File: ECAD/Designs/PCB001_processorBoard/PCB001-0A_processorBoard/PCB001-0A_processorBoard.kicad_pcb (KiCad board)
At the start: 2 copper layers, 59 parts, among them J1 USB_C_Receptacle_USB2.0_16P, SW1 BSL, SW2 RST, U1 W25Q128JVP, U2 RP2350B-QFN80, U3 BMI323, U4 MMC5983, U5 LG77LC, U6 NRF24L01_Breakout, Y1 ABM8-272-T3

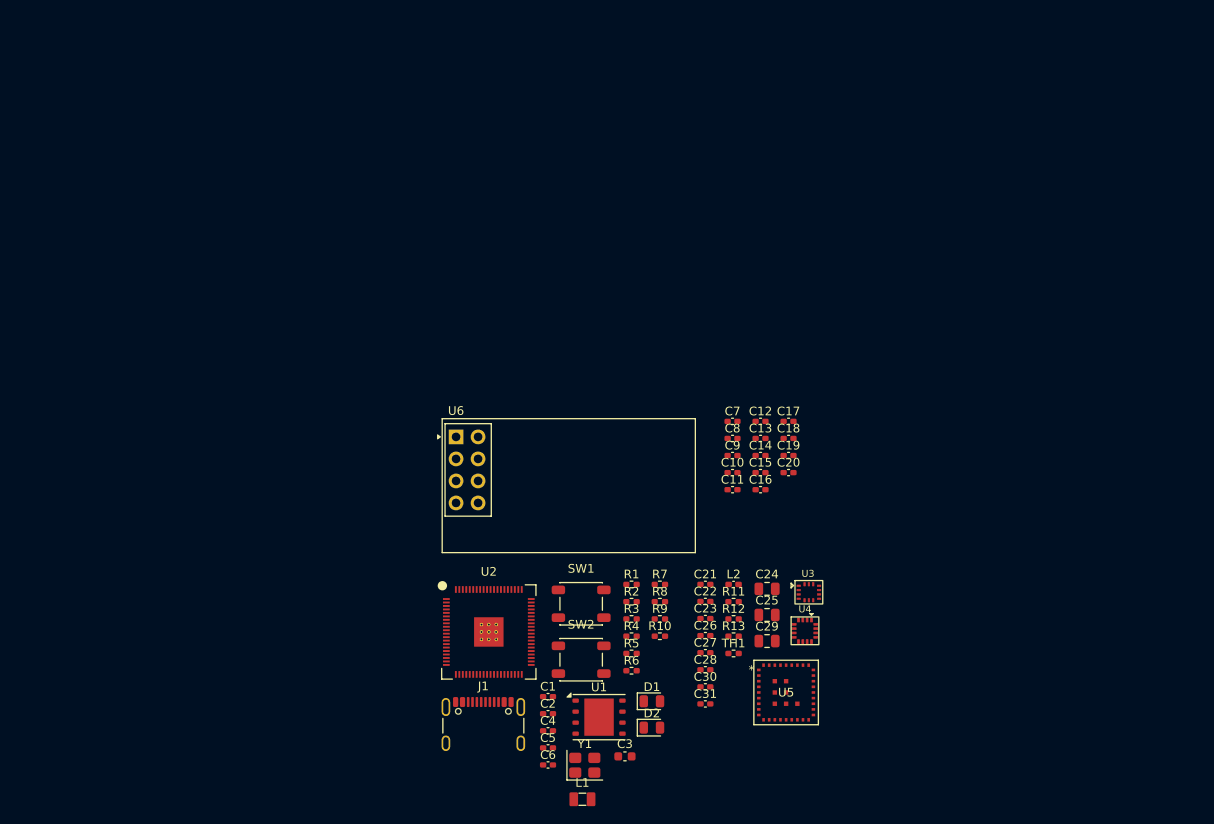
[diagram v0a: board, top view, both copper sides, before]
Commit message: added more connectors to the side of the PCB, added a basic power supply, and began putting parts on the PCB.
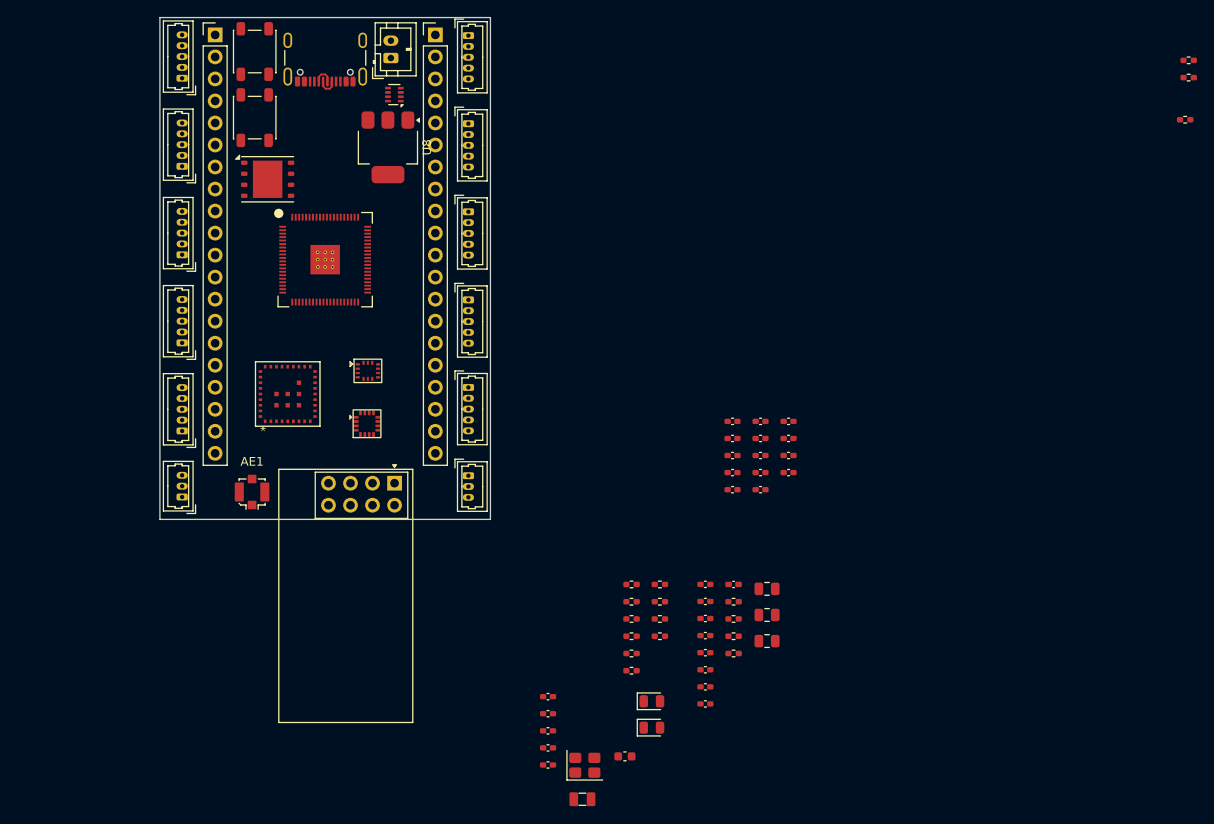
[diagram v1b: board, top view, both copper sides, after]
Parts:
- added AE1: Antenna_Shield, Connector_Coaxial:U.FL_Molex_MCRF_73412-0110_Vertical, F.Cu at (105.9, 101.0)
- added J1: Conn_01x20, Connector_PinHeader_2.54mm:PinHeader_1x20_P2.54mm_Vertical, F.Cu at (101.6, 48.3)
- added J10: ENVIRONMENT, Connector_Molex:Molex_PicoBlade_53047-0510_1x05_P1.25mm_Vertical, F.Cu at (97.8, 93.9)
- added J11: MOTOR0, Connector_Molex:Molex_PicoBlade_53047-0510_1x05_P1.25mm_Vertical, F.Cu at (130.8, 48.3)
- added J12: MOTOR1, Connector_Molex:Molex_PicoBlade_53047-0510_1x05_P1.25mm_Vertical, F.Cu at (130.8, 58.5)
- added J13: MOTOR2, Connector_Molex:Molex_PicoBlade_53047-0510_1x05_P1.25mm_Vertical, F.Cu at (130.8, 68.7)
- added J14: MOTOR3, Connector_Molex:Molex_PicoBlade_53047-0510_1x05_P1.25mm_Vertical, F.Cu at (130.8, 78.8)
- added J15: DISPLAY, Connector_Molex:Molex_PicoBlade_53047-0510_1x05_P1.25mm_Vertical, F.Cu at (130.8, 88.9)
- added J16: EXT_PWR, Connector_JST:JST_PH_B2B-PH-K_1x02_P2.00mm_Vertical, F.Cu at (121.9, 50.9)
- added J2: Conn_01x20, Connector_PinHeader_2.54mm:PinHeader_1x20_P2.54mm_Vertical, F.Cu at (127.0, 48.3)
- added J4: UART0, Connector_Molex:Molex_PicoBlade_53047-0310_1x03_P1.25mm_Vertical, F.Cu at (97.8, 101.6)
- added J5: UART1, Connector_Molex:Molex_PicoBlade_53047-0310_1x03_P1.25mm_Vertical, F.Cu at (130.8, 99.1)
- added J6: ULTRASONIC1, Connector_Molex:Molex_PicoBlade_53047-0510_1x05_P1.25mm_Vertical, F.Cu at (97.8, 73.6)
- added J7: ULTRASONIC2, Connector_Molex:Molex_PicoBlade_53047-0510_1x05_P1.25mm_Vertical, F.Cu at (97.8, 63.4)
- added J8: ULTRASONIC3, Connector_Molex:Molex_PicoBlade_53047-0510_1x05_P1.25mm_Vertical, F.Cu at (97.8, 53.3)
- added J9: ULTRASONIC0, Connector_Molex:Molex_PicoBlade_53047-0510_1x05_P1.25mm_Vertical, F.Cu at (97.8, 83.8)
- added R14: 10k, Resistor_SMD:R_0402_1005Metric_Pad0.72x0.64mm_HandSolder, F.Cu at (213.5, 58.0)
- added R15: 10k, Resistor_SMD:R_0402_1005Metric_Pad0.72x0.64mm_HandSolder, F.Cu at (213.9, 51.2)
- added R16: 10k, Resistor_SMD:R_0402_1005Metric_Pad0.72x0.64mm_HandSolder, F.Cu at (213.9, 53.2)
- added U7: LM66200, Package_TO_SOT_SMD:SOT-583-8, F.Cu at (122.3, 55.1)
- added U8: AZ1117-3.3, Package_TO_SOT_SMD:SOT-223, F.Cu at (121.5, 61.2)
- moved J3 81.0 mm to (114.3, 50.0), turned to 180 degrees
- moved SW1 74.0 mm to (106.2, 50.2), turned to 90 degrees
- moved SW2 73.0 mm to (106.2, 57.8), turned to 90 degrees
- moved U1 72.9 mm to (107.7, 64.9)
- moved U5 67.0 mm to (110.0, 89.7), turned to 90 degrees
- moved U3 56.9 mm to (119.2, 87.0)
- moved U4 55.9 mm to (119.1, 93.1), turned to 90 degrees
- moved U2 46.9 mm to (114.3, 74.2)
- moved U6 8.88 mm to (122.3, 100.0), turned to -90 degrees
- renumbered J1 to J3
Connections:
- net /GPIO10 renamed /main_processor/SPI1_SCK
- net /GPIO11 renamed /main_processor/SPI1_TX
- net /GPIO12 renamed /main_processor/SPI1_RX
- net /GPIO2 renamed /main_processor/UART0_TX
- net /GPIO3 renamed /main_processor/UART0_RX
- net /GPIO4 renamed /main_processor/UART1_TX
- net /GPIO5 renamed /main_processor/UART1_RX
- net /GPIO8 renamed /main_processor/SDA0
- net /GPIO9 renamed /main_processor/SCL0
- D2 pad 2: /GPIO25 -> /main_processor/LED_BUILTIN
- U2 pad 12: /GPIO13 -> unconnected-(U2-GPIO13-Pad12)
- U2 pad 13: /GPIO14 -> unconnected-(U2-GPIO14-Pad13)
- U2 pad 14: /GPIO15 -> unconnected-(U2-GPIO15-Pad14)
- U2 pad 16: /GPIO16 -> unconnected-(U2-GPIO16-Pad16)
- U2 pad 17: /GPIO17 -> unconnected-(U2-GPIO17-Pad17)
- U2 pad 18: /GPIO18 -> unconnected-(U2-GPIO18-Pad18)
- U2 pad 19: /GPIO19 -> unconnected-(U2-GPIO19-Pad19)
- U2 pad 20: /GPIO20 -> unconnected-(U2-GPIO20-Pad20)
- U2 pad 21: /GPIO21 -> unconnected-(U2-GPIO21-Pad21)
- U2 pad 22: /GPIO22 -> unconnected-(U2-GPIO22-Pad22)
- U2 pad 23: /GPIO23 -> unconnected-(U2-GPIO23-Pad23)
- U2 pad 25: /GPIO24 -> unconnected-(U2-GPIO24-Pad25)
- U2 pad 26: /GPIO25 -> unconnected-(U2-GPIO25-Pad26)
- U2 pad 27: /GPIO26 -> unconnected-(U2-GPIO26-Pad27)
- U2 pad 28: /GPIO27 -> unconnected-(U2-GPIO27-Pad28)
- U2 pad 3: /GPIO6 -> unconnected-(U2-GPIO6-Pad3)
- U2 pad 36: /GPIO28 -> unconnected-(U2-GPIO28-Pad36)
- U2 pad 37: /GPIO29 -> unconnected-(U2-GPIO29-Pad37)
- U2 pad 38: /GPIO30 -> unconnected-(U2-GPIO30-Pad38)
- U2 pad 39: /GPIO31 -> unconnected-(U2-GPIO31-Pad39)
- U2 pad 4: /GPIO7 -> unconnected-(U2-GPIO7-Pad4)
- U2 pad 40: /GPIO32 -> unconnected-(U2-GPIO32-Pad40)
- U2 pad 42: /GPIO33 -> unconnected-(U2-GPIO33-Pad42)
- U2 pad 43: /GPIO34 -> unconnected-(U2-GPIO34-Pad43)
- U2 pad 44: /GPIO35 -> unconnected-(U2-GPIO35-Pad44)
- U2 pad 45: /GPIO36 -> unconnected-(U2-GPIO36-Pad45)
- U2 pad 46: /GPIO37 -> unconnected-(U2-GPIO37-Pad46)
- U2 pad 47: /GPIO38 -> unconnected-(U2-GPIO38-Pad47)
- U2 pad 48: /GPIO39 -> unconnected-(U2-GPIO39-Pad48)
- U2 pad 49: /GPIO40 -> unconnected-(U2-GPIO40_ADC0-Pad49)
- U2 pad 52: /GPIO41 -> unconnected-(U2-GPIO41_ADC1-Pad52)
- U2 pad 53: /GPIO42 -> unconnected-(U2-GPIO42_ADC2-Pad53)
- U2 pad 54: /GPIO43 -> unconnected-(U2-GPIO43_ADC3-Pad54)
- U2 pad 55: /GPIO44 -> unconnected-(U2-GPIO44_ADC4-Pad55)
- U2 pad 56: /GPIO45 -> unconnected-(U2-GPIO45_ADC5-Pad56)
- U2 pad 57: /GPIO46 -> unconnected-(U2-GPIO46_ADC6-Pad57)
- U2 pad 58: /GPIO47 -> unconnected-(U2-GPIO47_ADC7-Pad58)
- U2 pad 77: /GPIO0 -> unconnected-(U2-GPIO0-Pad77)
- U2 pad 78: /GPIO1 -> unconnected-(U2-GPIO1-Pad78)
- U6 pad 1: unconnected-(U6-GND-Pad1) -> GND
- U6 pad 2: unconnected-(U6-VCC-Pad2) -> +3V3
- U6 pad 3: unconnected-(U6-CE-Pad3) -> /main_processor/NRF_CE
- U6 pad 4: unconnected-(U6-~{CSN}-Pad4) -> /main_processor/NRF_~{CS}
- U6 pad 5: unconnected-(U6-SCK-Pad5) -> /onBoardComms/SPI1_SCK
- U6 pad 6: unconnected-(U6-MOSI-Pad6) -> /onBoardComms/SPI1_TX
- U6 pad 7: unconnected-(U6-MISO-Pad7) -> /onBoardComms/SPI1_RX
- U6 pad 8: unconnected-(U6-IRQ-Pad8) -> /main_processor/NRF_IRQ
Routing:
- net /main_processor/D-: track 0.00 -> 2.35 mm
- net /main_processor/D+: track 0.00 -> 2.34 mm
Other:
- board outline added: 38.1 x 57.9 mm

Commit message: updated schematics
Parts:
- removed J16: EXT_PWR, Connector_JST:JST_PH_B2B-PH-K_1x02_P2.00mm_Vertical
- removed the U8 at (121.5, 61.2)
- added C3: 100nF, Capacitor_SMD:C_0402_1005Metric_Pad0.74x0.62mm_HandSolder, F.Cu at (111.6, 56.1)
- added C33: 100nF, Capacitor_SMD:C_0402_1005Metric_Pad0.74x0.62mm_HandSolder, F.Cu at (79.7, 79.4)
- added C34: 100nF, Capacitor_SMD:C_0402_1005Metric_Pad0.74x0.62mm_HandSolder, F.Cu at (79.7, 81.4)
- added H1: M2, MountingHole:MountingHole_2.2mm_M2, F.Cu at (106.2, 75.5)
- added H2: M2, MountingHole:MountingHole_2.2mm_M2, F.Cu at (122.4, 75.2)
- added H3: M2, MountingHole:MountingHole_2.2mm_M2, F.Cu at (138.9, 78.1)
- added H4: M2, MountingHole:MountingHole_2.2mm_M2, F.Cu at (138.9, 84.1)
- added R15: 10k, Resistor_SMD:R_0402_1005Metric_Pad0.72x0.64mm_HandSolder, F.Cu at (83.0, 79.5)
- added U7: TXS0108EPW, Package_SO:TSSOP-20_4.4x6.5mm_P0.65mm, F.Cu at (116.0, 80.9)
- added U9: TLV75533PDRV, Package_SON:WSON-6-1EP_2x2mm_P0.65mm_EP1x1.6mm, F.Cu at (122.7, 58.3)
- J1, J2: moved to B.Cu
- moved C4 81.1 mm to (120.5, 55.5), turned to 90 degrees
- moved R10 70.2 mm to (115.0, 58.6), turned to -90 degrees
- moved R3 70.0 mm to (112.8, 56.1), turned to -90 degrees
- moved R9 69.1 mm to (113.9, 58.6), turned to -90 degrees
- moved R2 66.5 mm to (116.2, 56.2), turned to -90 degrees
- moved Y1 65.3 mm to (112.3, 75.6)
- moved C8 59.4 mm to (112.8, 58.6), turned to 90 degrees
- moved SW2 18.0 mm to (122.4, 50.1)
- moved U1 6.99 mm to (107.5, 57.9)
- moved U2 6.95 mm to (113.9, 67.2)
- moved U8 0.55 mm to (122.7, 55.5)
- turned J1 to 180 degrees
- turned J2 to 180 degrees
- renumbered C9 to C10, C10 to C11, C11 to C12, C12 to C13, C13 to C14, C14 to C15, C15 to C16, C16 to C17, C17 to C18, C18 to C19, C19 to C20, C20 to C21, C21 to C22, C22 to C23, C23 to C24, C24 to C25, C25 to C26, C26 to C27, C27 to C28, C28 to C29, C29 to C30, C30 to C31, C31 to C32, C3 to C4, C4 to C5, C5 to C6, C6 to C7, C7 to C8, C8 to C9, J9 to J6, J6 to J7, J7 to J8, J8 to J9, R15 to R16, R16 to R17, U7 to U8
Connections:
- J6 pad 1: +3V3 -> +5V
- J6 pad 3: /main_processor/TRIG0 -> /offBoardSensors/TRIG0_5V
- J6 pad 4: /main_processor/ECHO0 -> /offBoardSensors/ECHO0_5V
- J7 pad 1: +3V3 -> +5V
- J7 pad 3: /main_processor/TRIG1 -> /offBoardSensors/TRIG1_5V
- J7 pad 4: /main_processor/ECHO1 -> /offBoardSensors/ECHO1_5V
- J8 pad 1: +3V3 -> +5V
- J8 pad 3: /main_processor/TRIG2 -> /offBoardSensors/TRIG2_5V
- J8 pad 4: /main_processor/ECHO2 -> /offBoardSensors/ECHO2_5V
- J9 pad 1: +3V3 -> +5V
- J9 pad 3: /main_processor/TRIG3 -> /offBoardSensors/TRIG3_5V
- J9 pad 4: /main_processor/ECHO3 -> /offBoardSensors/ECHO3_5V
- R17 pad 1: Net-(U8-VI) -> +5V
- U8 pad 2: Net-(U8-VI) -> +5V
- U8 pad 3: +5V -> /power_supply/5V IN
- U8 pad 7: Net-(U8-VI) -> +5V
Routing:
- net /main_processor/VBUS: track 0.00 -> 7.09 mm
- net /main_processor/D-: track 2.35 -> 0.00 mm
- net Net-(J3-CC1): track 0.00 -> 2.23 mm
- net Net-(J3-CC2): track 0.00 -> 2.00 mm
- net +3V3: track 0.00 -> 1.64 mm, vias 0 -> 1
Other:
- copper layers 2 -> 4
